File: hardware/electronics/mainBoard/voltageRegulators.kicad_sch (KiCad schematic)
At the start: 40 parts, among them J18 Conn_01x04_Pin, J19 Conn_01x04_Pin, Q1 BSS138-7-F, Q2 BSS138-7-F, U21 TPS543B25, U22 TPS62A01

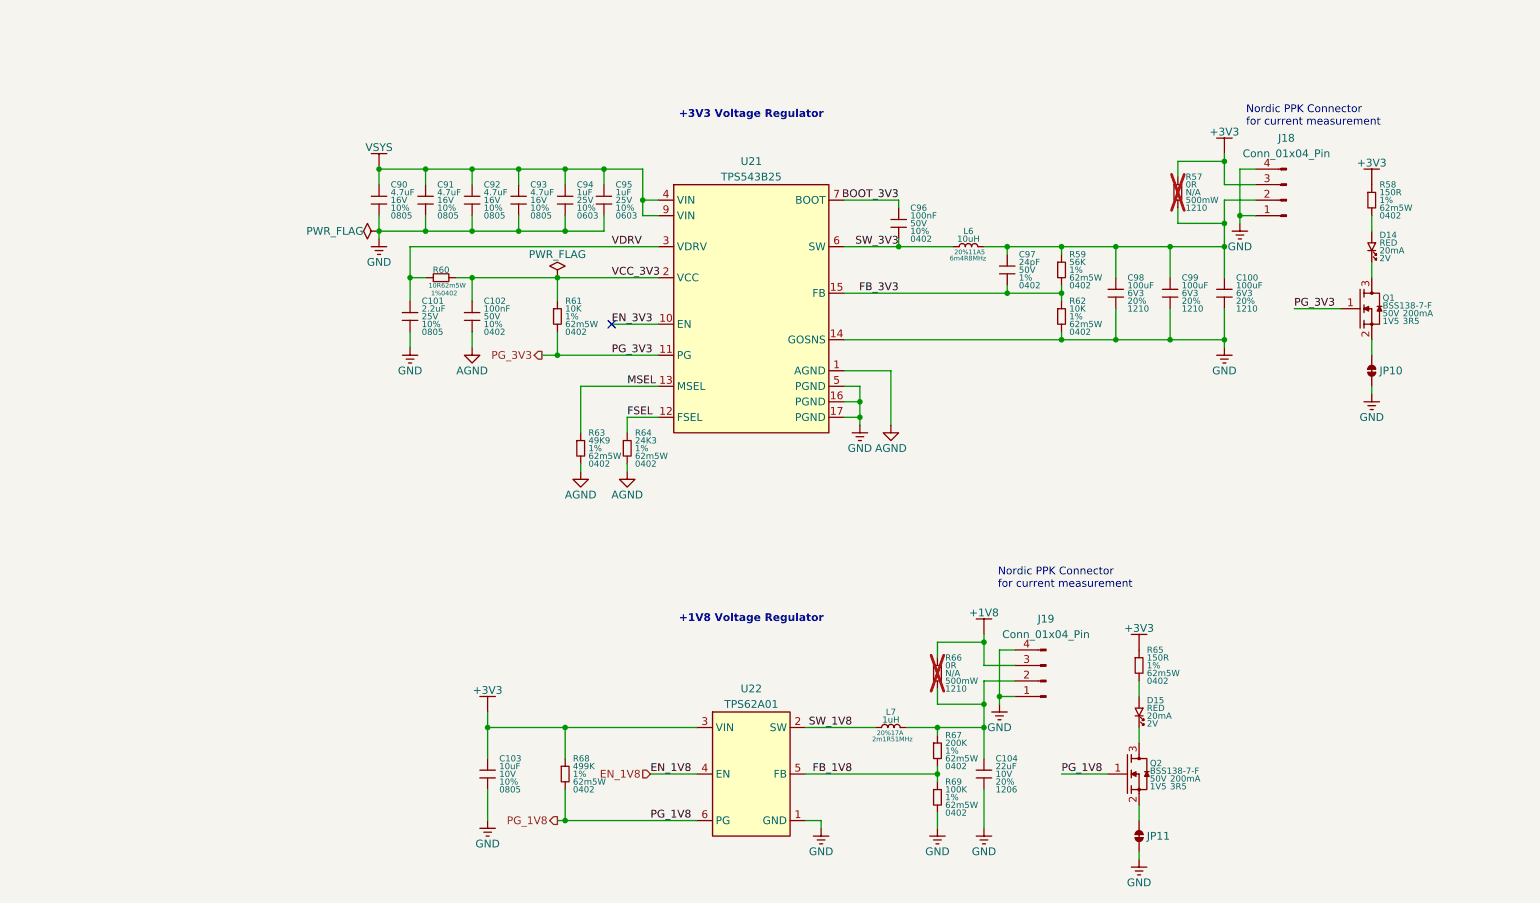
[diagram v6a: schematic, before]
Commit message: replaced 3V3 reg with more efficient one
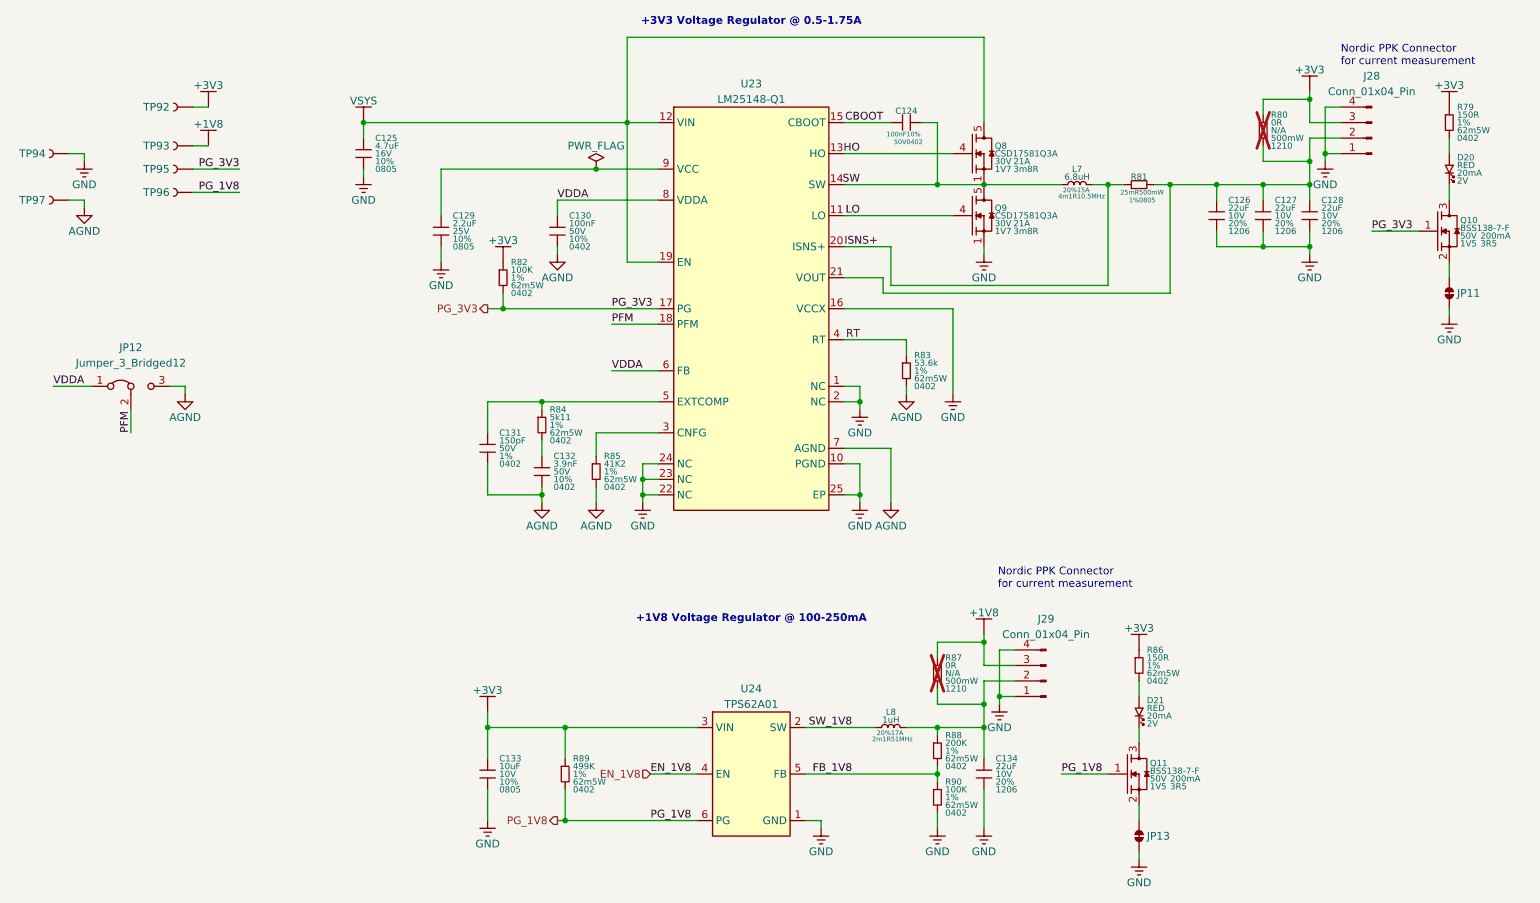
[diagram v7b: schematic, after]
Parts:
- removed C100, C98, C99: 100uF, symbol lib_sch:C
- removed C101: 2.2uF, symbol lib_sch:C
- removed C102, C96: 100nF, symbol lib_sch:C
- removed C90, C91, C92, C93: 4.7uF, symbol lib_sch:C
- removed C94, C95: 1uF, symbol lib_sch:C
- removed C97: 24pF, symbol lib_sch:C
- removed L6: 10uH, symbol lib_sch:L_horizontal
- removed R59: 56K, symbol lib_sch:R
- removed R60: 10R, symbol lib_sch:R_horizontal
- removed R61, R62: 10K, symbol lib_sch:R
- removed R63: 49K9, symbol lib_sch:R
- removed R64: 24K3, symbol lib_sch:R
- removed U21: TPS543B25, symbol lib_sch:TPS543B25
- added C124: 100nF, symbol lib_sch:C_horizontal
- added C125: 4.7uF, symbol lib_sch:C
- added C126, C127, C128: 22uF, symbol lib_sch:C
- added C129: 2.2uF, symbol lib_sch:C
- added C130: 100nF, symbol lib_sch:C
- added C131: 150pF, symbol lib_sch:C
- added C132: 3.9nF, symbol lib_sch:C
- added JP12: Jumper_3_Bridged12, symbol lib_sch:Jumper_3_Bridged12
- added L7: 6.8uH, symbol lib_sch:L_horizontal
- added Q8, Q9: CSD17581Q3A, symbol lib_sch:NMOS_SGD_PWR
- added R81: 25mR, symbol lib_sch:R_horizontal
- added R82: 100K, symbol lib_sch:R
- added R83: 53.6k, symbol lib_sch:R
- added R84: 5k11, symbol lib_sch:R
- added R85: 41K2, symbol lib_sch:R
- added TP92, TP93, TP95, TP96: ~, symbol lib_sch:Testpoint
- added TP94, TP97: RCWCTE, symbol lib_sch:Testpoint
- added U23: LM25148-Q1, symbol lib_sch:LM25148
- Q10: renamed from Q1; symbol .DS-Transistors:NMOS_GSD -> lib_sch:NMOS_GSD
- Q11: renamed from Q2; symbol .DS-Transistors:NMOS_GSD -> lib_sch:NMOS_GSD
- renumbered C103 to C133, C104 to C134, D14 to D20, D15 to D21, J18 to J28, J19 to J29, JP10 to JP11, JP11 to JP13, L7 to L8, R58 to R79, R57 to R80, R65 to R86, R66 to R87, R67 to R88, R68 to R89, R69 to R90, U22 to U24
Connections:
- net +1V8: now also TP93.1
- net +3V3: now also R82.1, TP92.1
- net AGND: now also C130.2, C131.2, C132.2, JP12.3 (B), R83.2, R85.2, TP97.1, U23.7 (AGND)
- net GND: now also C125.2, C126.2, C127.2, C128.2, C129.2, Q9.1, Q9.2, Q9.3, TP94.1, U23.1 (NC), U23.10 (PGND), U23.16 (VCCX), U23.2 (NC), U23.22 (NC), U23.23 (NC), U23.24 (NC), U23.25 (EP)
- net PG_1V8: now also TP96.1
- net PG_3V3: now also R82.2, TP95.1, U23.17 (PG)
- net VSYS: now also C125.1, Q8.5, Q8.6, Q8.7, Q8.8, U23.12 (VIN), U23.19 (EN)
- net at J28.2 (Pin_2), R80.2: now also C126.1, C127.1, C128.1, R81.2, U23.21 (VOUT)
- new net: R85.1, U23.3 (CNFG)
- new net: C132.1, R84.2
- new net: C129.1, U23.9 (VCC)
- new net: C131.1, R84.1, U23.5 (EXTCOMP)
- new net CBOOT: C124.1, U23.15 (CBOOT)
- new net HO: Q8.4, U23.13 (HO)
- new net ISNS+: L7.2, R81.1, U23.20 (ISNS+)
- new net LO: Q9.4, U23.11 (LO)
- new net PFM: JP12.2 (C), U23.18 (PFM)
- new net RT: R83.1, U23.4 (RT)
- new net SW: C124.2, L7.1, Q8.1, Q8.2, Q8.3, Q9.5, Q9.6, Q9.7, Q9.8, U23.14 (SW)
- new net VDDA: C130.1, JP12.1 (A), U23.6 (FB), U23.8 (VDDA)
- no-connect marks 1 -> 0
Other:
- note added: "+1V8 Voltage Regulator @ 100-250mA"
- note added: "+3V3 Voltage Regulator @ 0.5-1.75A"
- note removed: "+1V8 Voltage Regulator"
- note removed: "+3V3 Voltage Regulator"
- moved on the sheet: D20, J28, JP11, Q10, R79, R80

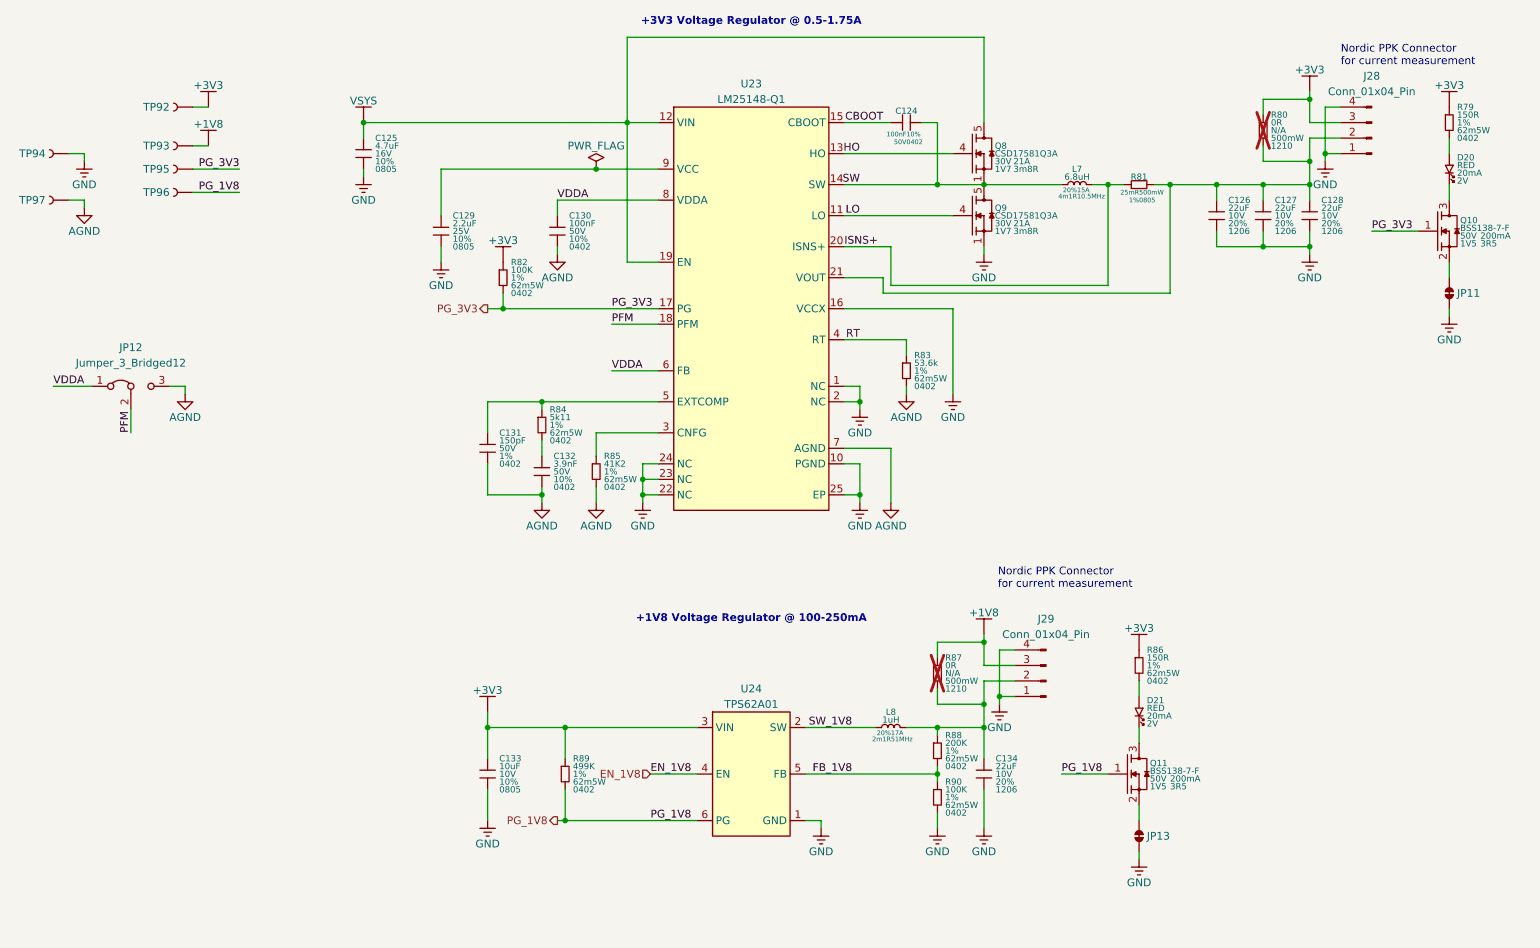
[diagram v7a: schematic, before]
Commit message: added comments for vregs
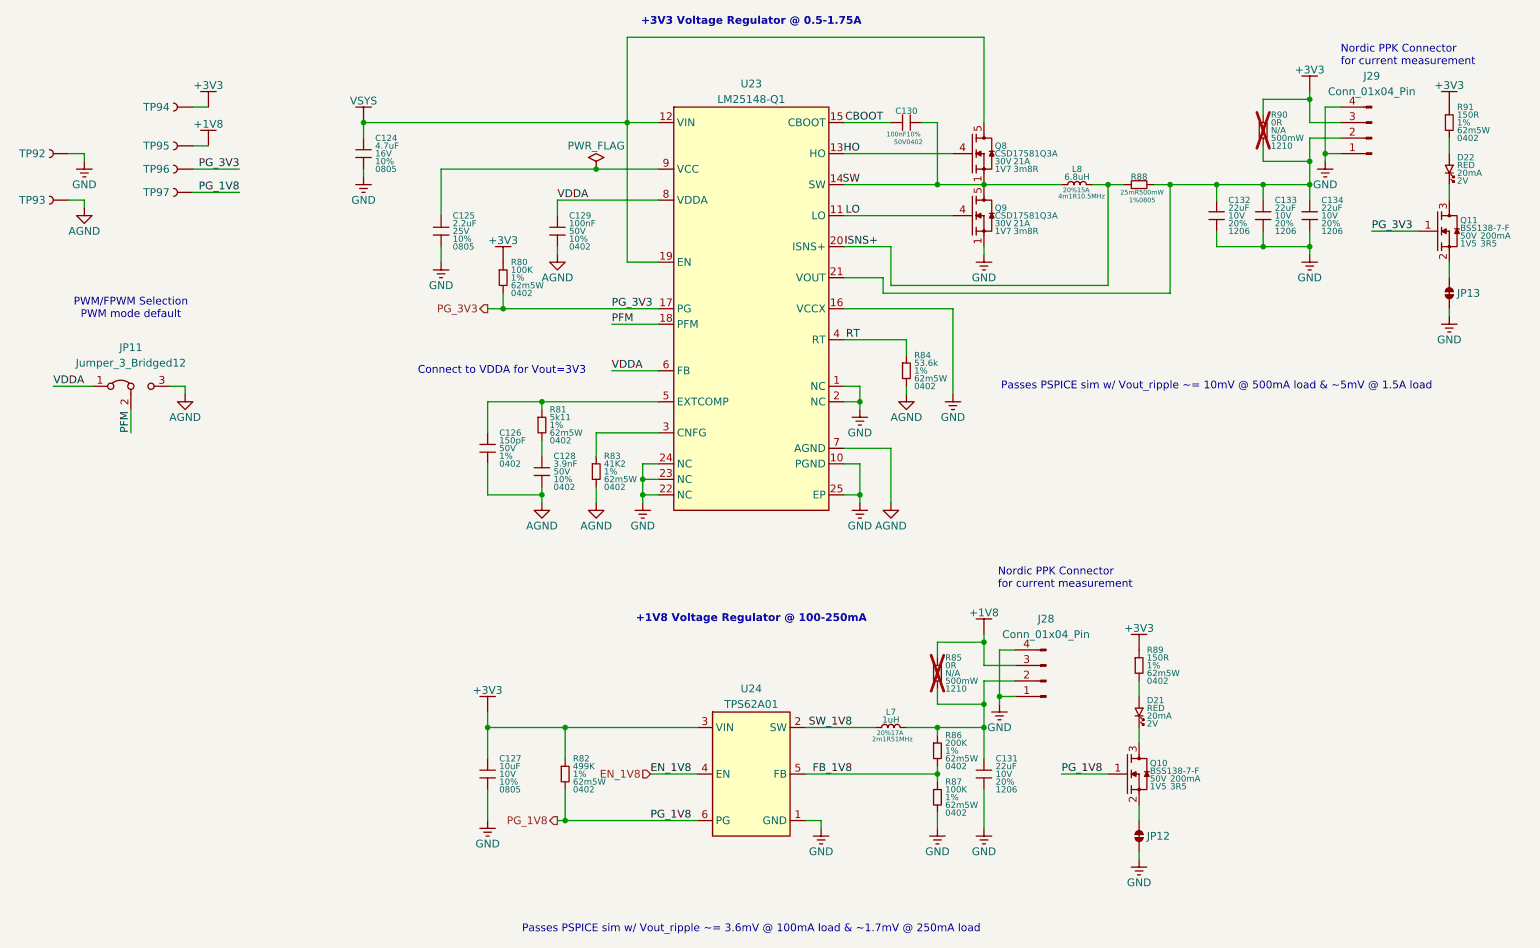
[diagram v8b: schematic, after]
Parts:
- renumbered C125 to C124, C129 to C125, C131 to C126, C133 to C127, C132 to C128, C130 to C129, C124 to C130, C134 to C131, C126 to C132, C127 to C133, C128 to C134, D20 to D22, J29 to J28, J28 to J29, JP12 to JP11, JP13 to JP12, JP11 to JP13, L8 to L7, L7 to L8, Q11 to Q10, Q10 to Q11, R82 to R80, R84 to R81, R89 to R82, R85 to R83, R83 to R84, R87 to R85, R88 to R86, R90 to R87, R81 to R88, R86 to R89, R80 to R90, R79 to R91, TP94 to TP92, TP97 to TP93, TP92 to TP94, TP93 to TP95, TP95 to TP96, TP96 to TP97
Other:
- note added: "Connect to VDDA for Vout=3V3"
- note added: "PWM/FPWM Selection PWM mode default"
- note added: "Passes PSPICE sim w/ Vout_ripple ~= 10mV @ 500mA load & ~5mV @ 1.5A load"
- note added: "Passes PSPICE sim w/ Vout_ripple ~= 3.6mV @ 100mA load & ~1.7mV @ 250mA load"
